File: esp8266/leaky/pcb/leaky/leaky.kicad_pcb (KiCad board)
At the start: 2 copper layers, 100 x 100 mm, 31 parts, among them J1 UART, J2 extra pins, Q1 BC327, SW1 sensing top, SW2 sensing bot, U1 DD0405MA, U2 ESP-12F

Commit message: leaky: More repos
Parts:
- moved TP1 87.7 mm to (19.6, 137.7)
- moved TP2 87.7 mm to (16.4, 127.5)
- moved TP3 87.7 mm to (16.4, 130.5)
- moved TP5 87.7 mm to (19.4, 129.0)
- moved SW1 6.41 mm to (70.2, 94.0)
- moved C2 5.22 mm to (52.6, 100.1), turned to 0 degrees
- moved JP2 1.91 mm to (58.0, 104.9)
- moved C3 0.39 mm to (51.8, 112.7)
- moved R3 0.20 mm to (55.6, 113.6)

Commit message: leaky: Test routing
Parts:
- removed SW2: sensing bot, Connector_PinHeader_2.54mm:PinHeader_1x02_P2.54mm_Vertical
- SW1: value sensing top -> sensing loop
- moved SW1 22.6 mm to (68.3, 116.5), turned to 270 degrees
- moved R1 1.00 mm to (69.0, 106.3), turned to 270 degrees
- moved Q1 0.25 mm to (65.2, 107.4)
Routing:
- net Net-(R1-Pad2): track 0.00 -> 187.1 mm
- net Net-(Q1-Pad2): track 0.00 -> 4.19 mm
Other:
- net class Power: via_dia 0.8 -> 1; via_drill 0.4 -> 0.8
- net class Sensing added: clearance 0.5, trace_width 1, via_dia 1, via_drill 0.8
- net class Signal: via_dia 1 -> 0.8; via_drill 0.8 -> 0.4

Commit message: leaky: Start working on bat footprint
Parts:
- BT1: footprint Battery:BatteryHolder_Keystone_2462_2xAA -> _my:BatteryHolder_Keystone_2462_2xAA

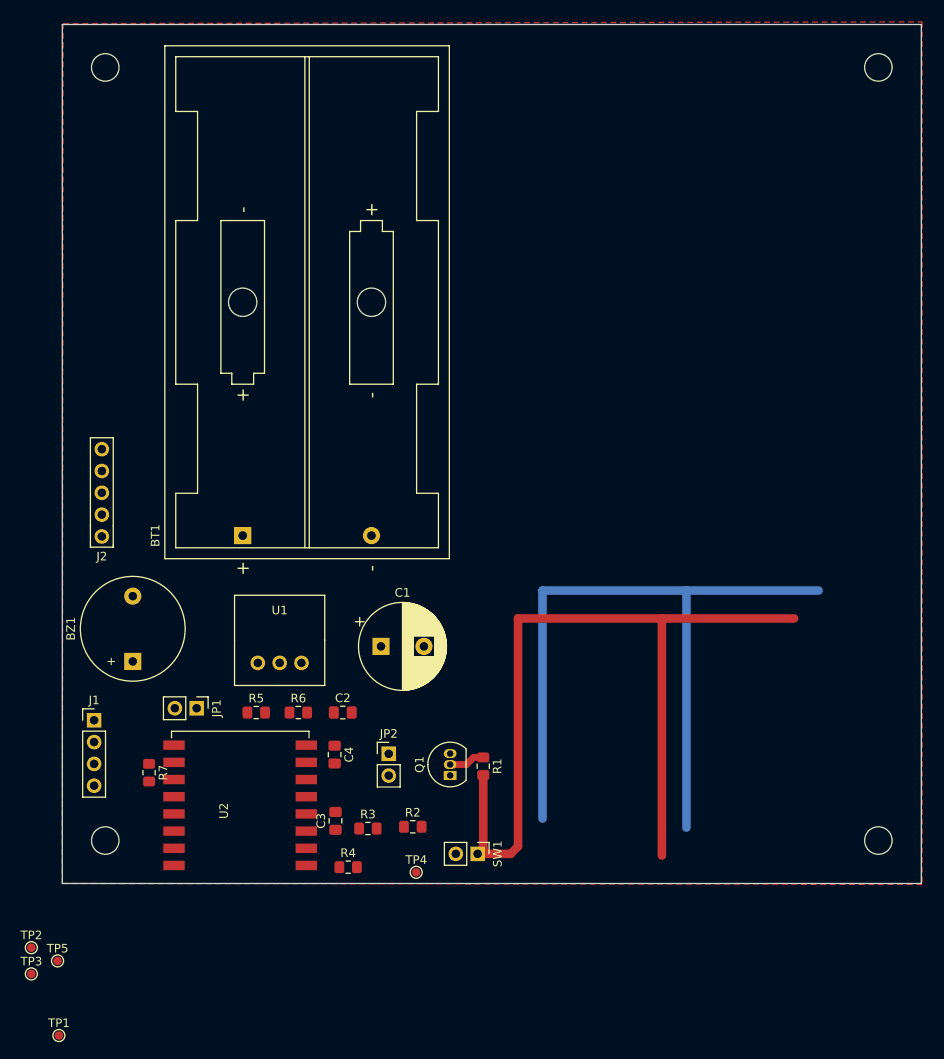
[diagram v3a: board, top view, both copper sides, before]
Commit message: leaky: Add bat footprint
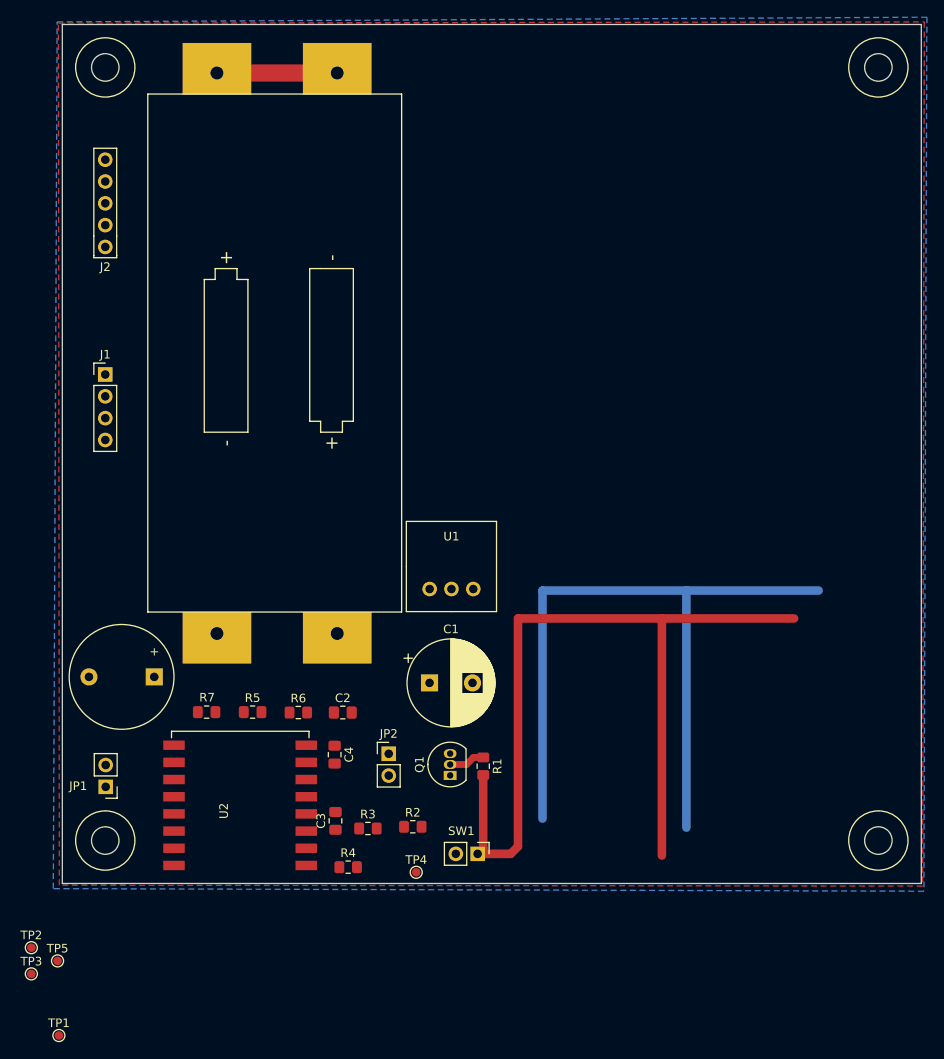
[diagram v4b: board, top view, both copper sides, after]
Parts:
- H1, H2, H3, H4: footprint MountingHole:MountingHole_3.2mm_M3 -> _my:MountingHole_3.2mm_M3
- moved J1 40.3 mm to (25.0, 60.8)
- moved J2 33.7 mm to (25.0, 45.9)
- moved U1 21.8 mm to (65.3, 78.1)
- moved BT1 20.5 mm to (59.5, 88.4)
- moved JP1 14.0 mm to (25.1, 108.8), turned to 180 degrees
- moved R7 9.73 mm to (36.8, 100.0), turned to 180 degrees
- moved C1 7.07 mm to (62.8, 96.7)
- moved BZ1 3.08 mm to (30.7, 96.0), turned to 180 degrees
- moved R5 0.43 mm to (42.1, 100.0)
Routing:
- net VBUS: track 0.00 -> 14.0 mm
- added copper zone on B.Cu, net GND

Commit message: leaky: Adjust silk screen
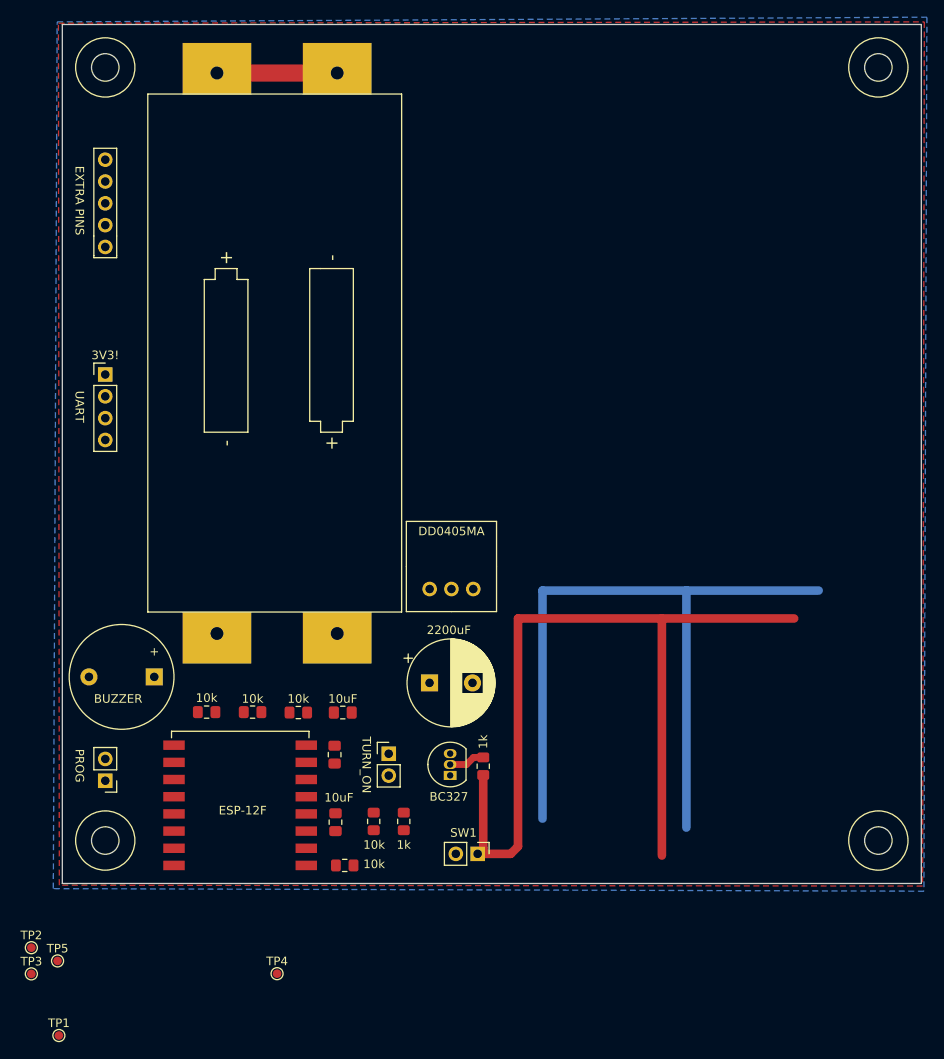
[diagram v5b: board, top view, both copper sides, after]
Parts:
- moved TP4 20.0 mm to (45.0, 130.5)
- moved R2 1.22 mm to (59.8, 112.8), turned to 270 degrees
- moved R3 1.07 mm to (56.2, 112.8), turned to 90 degrees
- moved JP1 0.71 mm to (25.0, 108.0)
- moved R4 0.45 mm to (52.9, 117.9)
- moved C3 0.15 mm to (51.8, 112.9)
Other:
- board text added: "3V3!"
- board text added: "BUZZER"
- board text added: "EXTRA PINS"

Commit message: leaky: Adjust cap
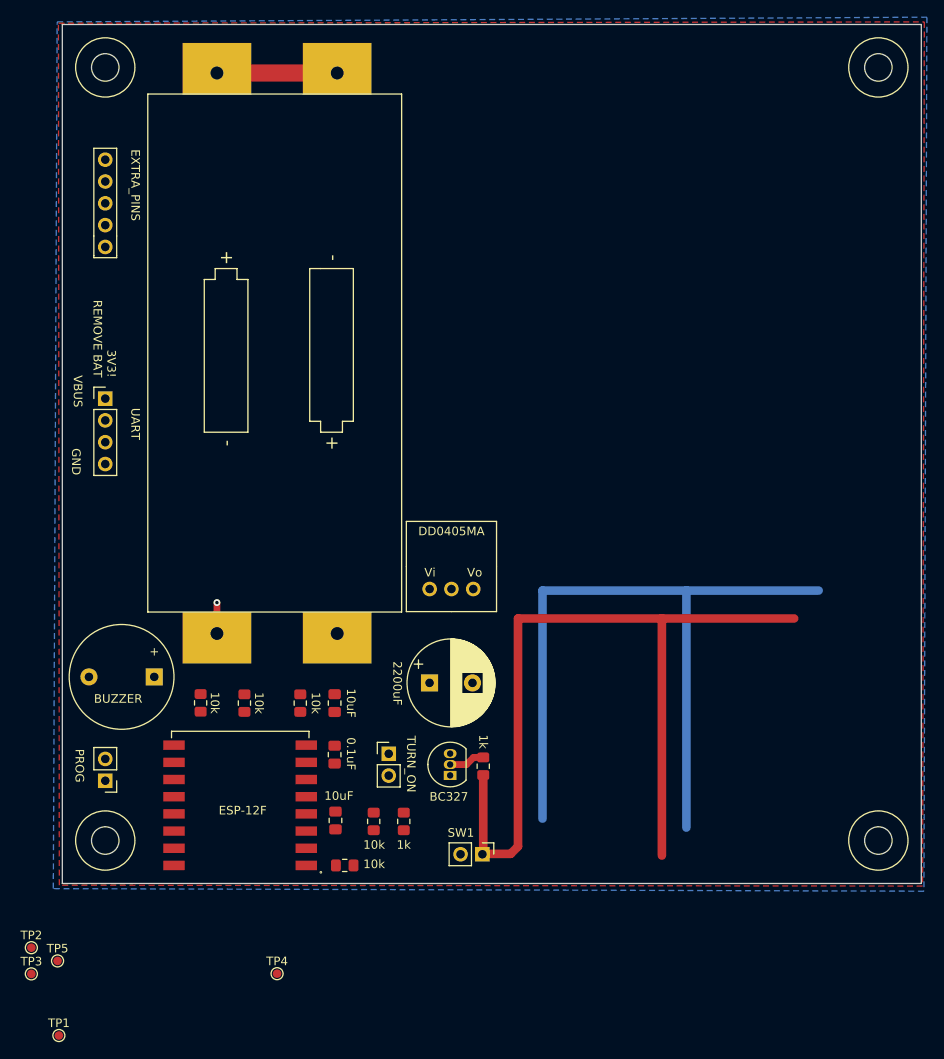
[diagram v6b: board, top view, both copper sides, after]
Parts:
- C1: footprint Capacitor_THT:CP_Radial_D10.0mm_P5.00mm -> _my:CP_Radial_D10.0mm_P5.00mm
- moved J1 2.80 mm to (25.0, 63.5)
- moved C2 1.45 mm to (51.7, 99.0), turned to 90 degrees
- moved R5 1.42 mm to (41.2, 99.0), turned to 270 degrees
- moved R7 1.28 mm to (36.1, 99.0), turned to 90 degrees
- moved R6 1.12 mm to (47.7, 99.0), turned to 270 degrees
- moved SW1 0.55 mm to (68.9, 116.6)
- moved C3 0.20 mm to (51.8, 112.7)
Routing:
- net GND: track 0.00 -> 3.60 mm, vias 0 -> 1
- net Net-(R1-Pad2): track 187.1 -> 185.6 mm
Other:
- board text added: "3V3! REMOVE BAT"
- board text added: "EXTRA_PINS"
- board text added: "GND"
- board text added: "VBUS"
- board text added: "Vi"
- board text added: "Vo"
- board text removed: "3V3!"
- board text removed: "EXTRA PINS"

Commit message: leaky: Update schema
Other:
- board text added: "12"
- board text added: "13"
- board text added: "14"
- board text added: "16"
- board text added: "4"
- board text added: "RX"
- board text added: "TX"

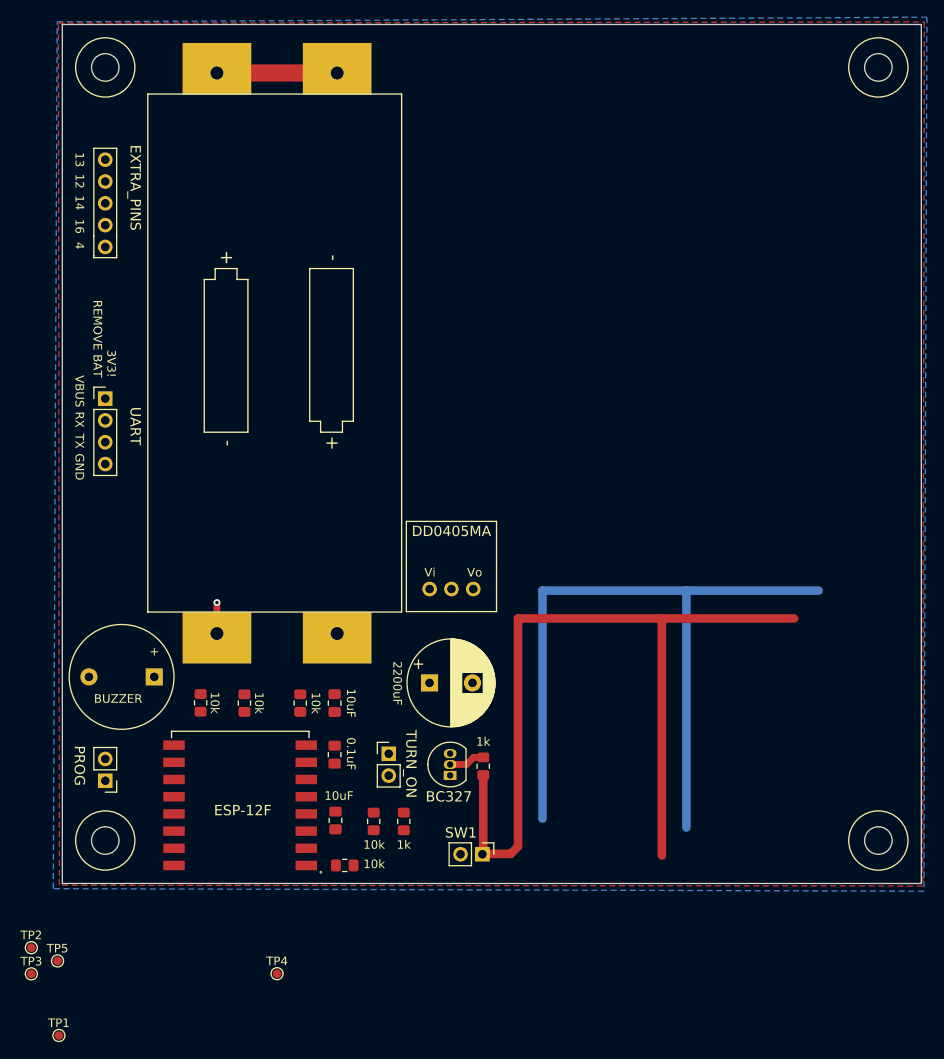
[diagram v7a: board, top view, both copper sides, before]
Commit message: leaky: Position test points
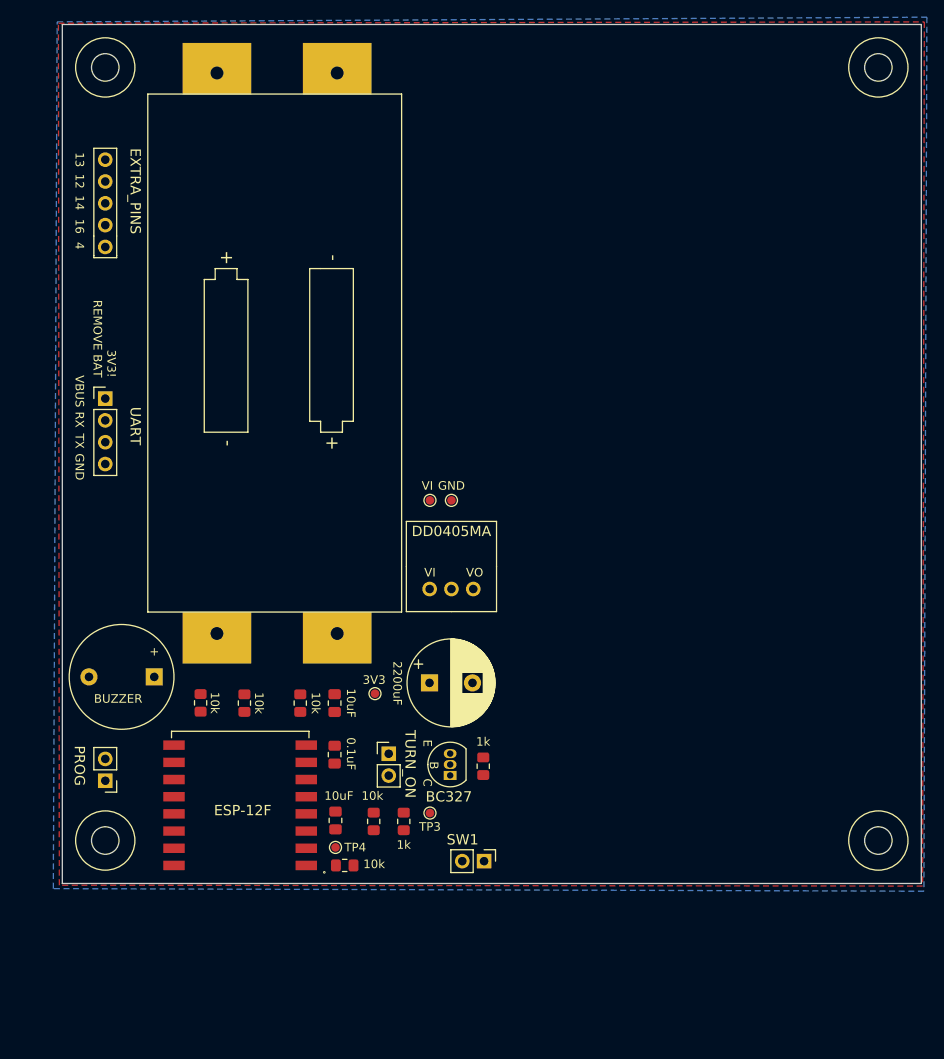
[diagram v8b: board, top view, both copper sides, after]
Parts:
- Q1: footprint Package_TO_SOT_THT:TO-92_Inline -> _my:TO-92_Inline
- moved TP1 77.3 mm to (65.3, 75.4)
- moved TP2 69.8 mm to (62.8, 75.4)
- moved TP3 50.0 mm to (62.8, 111.8)
- moved TP5 48.3 mm to (56.4, 97.9)
- moved TP4 16.2 mm to (51.8, 115.8)
- moved SW1 0.82 mm to (69.1, 117.4)
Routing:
- net Net-(R1-Pad2): track 185.6 -> 0.00 mm
- net VBUS: track 14.0 -> 0.00 mm
- net Net-(Q1-Pad2): track 4.19 -> 0.00 mm
- net GND: track 3.60 -> 0.00 mm, vias 1 -> 0
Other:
- board text added: "3V3"
- board text added: "VI"
- board text added: "VO"
- board text removed: "Vi"
- board text removed: "Vo"
